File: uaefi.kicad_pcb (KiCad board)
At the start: 4 copper layers, 100 x 100 mm, 171 parts, among them J1 Conn_02x02_Odd_Even, J10 5569-16A2, J11 Conn_02x02_Odd_Even, J12 Conn_02x02_Odd_Even, J13 Conn_02x02_Odd_Even, J14 Conn_02x02_Odd_Even, J15 Conn_02x02_Odd_Even, J16 Conn_02x02_Odd_Even, J17 Conn_02x02_Odd_Even, J18 Conn_02x02_Odd_Even, J19 Conn_02x02_Odd_Even, J2 5569-20A2, J20 Conn_02x02_Odd_Even, J21 Conn_02x02_Odd_Even, J22 Conn_02x02_Odd_Even, J24 Conn_02x02_Odd_Even, J3 5569-06A2, J4 5569-08A2, J5 5569-18A2, J6 Conn_01x06, J7 Conn_01x05_Male, J8 USB_B_Mini, J9 USB_C, M1 Module-power_12and5V-0.3, M2 Module-knock-0.2, M3 Module-vr-discrete-0.5, M4 Module-vr-max9924-0.1, M5 Module-wbo-0.6, M6 Module:mega-mcu100/0.3, M7 Module-can-0.1, P1 Pad, P15 Pad, P16 Pad, P17 Pad, P18 Pad, P2 Pad, P3 Pad, P4 Pad, P5 Pad, P6 Pad, P7 Pad, P8 Pad, Q10 ISL9V3040D3ST, Q11 ISL9V3040D3ST, Q12 ISL9V3040D3ST, Q7 ISL9V3040D3ST, Q8 ISL9V3040D3ST, Q9 ISL9V3040D3ST, U1 TLE9201SG, U10 VNLD5160TR-E, U11 VNLD5160TR-E, U2 TLE9201SG, U3 MPX4/MPXH6400_MAP, U4 MAX31855KASA, U5 JDY-33, U6 VNLD5160TR-E, U7 VNLD5160TR-E, U8 VNLD5160TR-E, U9 VNLD5160TR-E

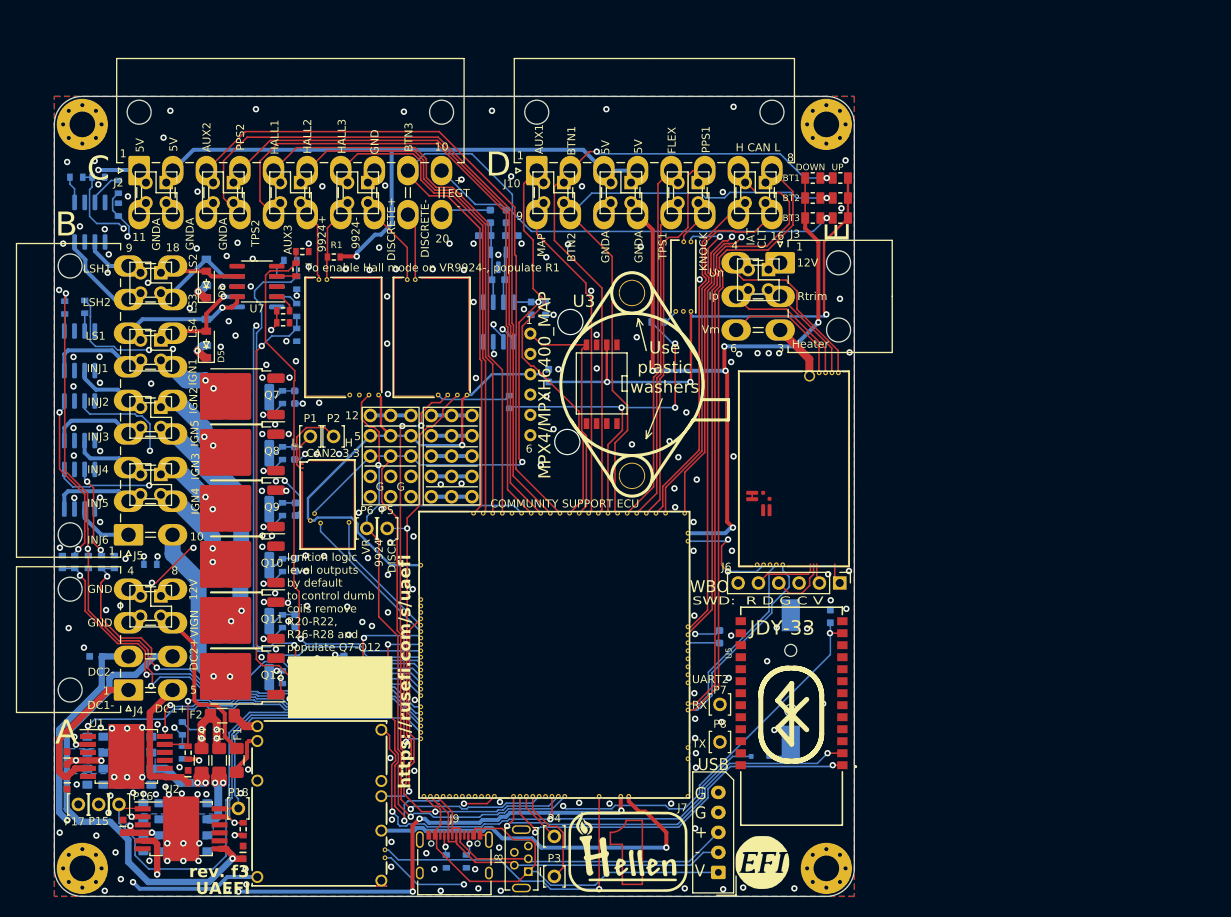
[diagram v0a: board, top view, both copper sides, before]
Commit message: uaefi-moto: PCB prepared for routing, bluetooth fix caps [skip ci]
Schematic:
- breakout pin headers J1, J11-J24 removed (never populated)
- C40 47uF on +5V and C41 470uF on +3.3VA for the JDY-33 power-up issue
- ERC 0 errors, no existing net changed, connector pins match spreadsheet

PCB:
- old Mini-Fit connectors, DC drivers, F3/F4, breakout headers and the
  routes that only led to them removed
- board enlarged to 145 x 110 mm (right: EGT/M8, top: Superseal pin depth)
- J30/J31, F11, M8, J32-J35, four MAX31855 groups, C40/C41 pre-placed
- DRC: 0 errors except library courtyard of the Superseal footprint,
  schematic parity 0, 138 unconnected items left to route

Co-Authored-By: Claude Opus 5.5 <noreply@anthropic.com>
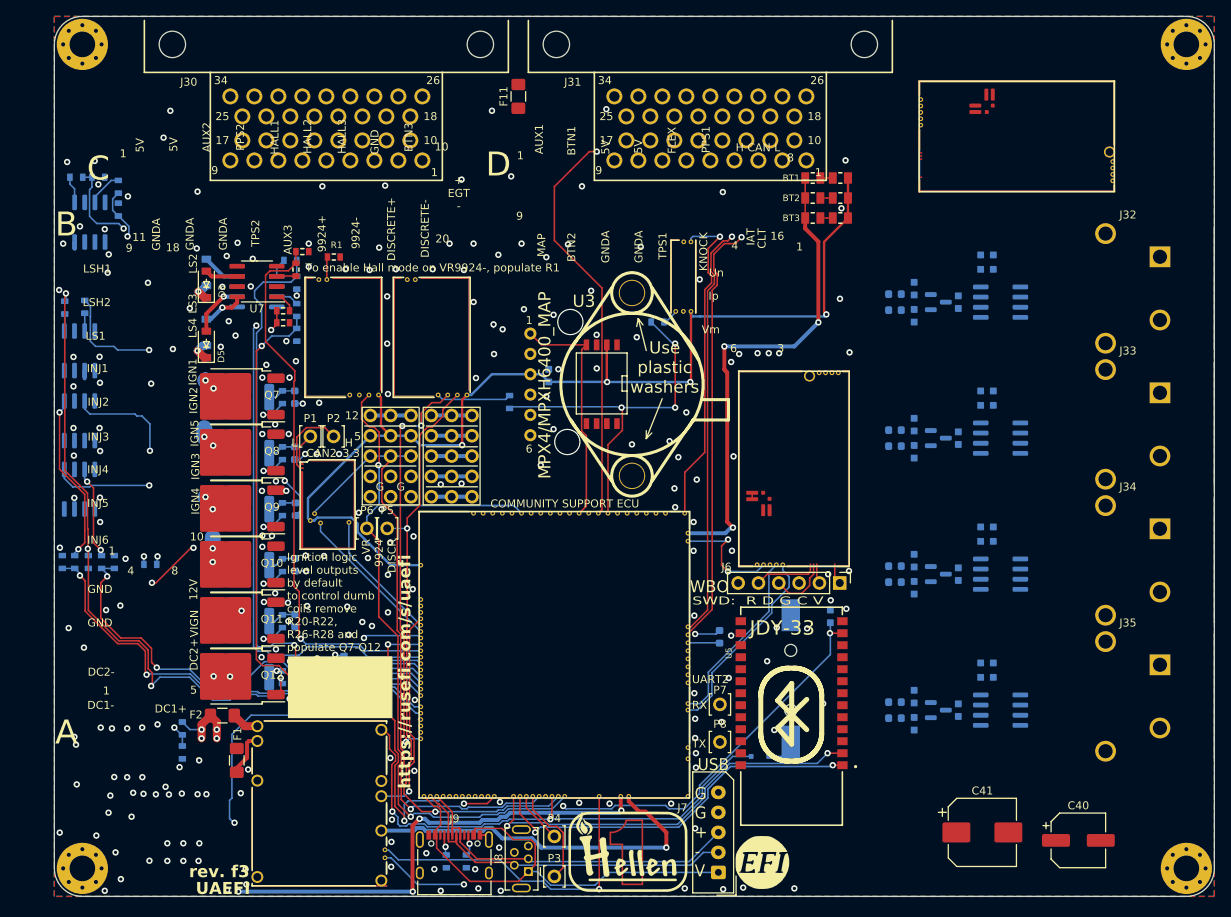
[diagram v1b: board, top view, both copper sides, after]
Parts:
- removed C1, C10, C14, C15, C16, C17, C18, C19, C2, C20, C21, C22, C23, C3, C4, C5, C6, C7, C8, C9: 10u, hellen-one-common:C0805
- removed C11, C24: 100n, hellen-one-common:C0603
- removed C12, C13, C25, C26: 10n, hellen-one-common:C0603
- removed F3, F4: Fuse, Fuse:Fuse_1206_3216Metric_Pad1.42x1.75mm_HandSolder
- removed J1, J11, J12, J13, J14, J15, J16, J17, J18, J19, J20, J21, J22, J24: Conn_02x02_Odd_Even, Connector_PinSocket_2.54mm:PinSocket_2x02_P2.54mm_Vertical
- removed J10: 5569-16A2, Connector_Molex:Molex_Mini-Fit_Jr_5569-16A2_2x08_P4.20mm_Horizontal
- removed J2: 5569-20A2, Connector_Molex:Molex_Mini-Fit_Jr_5569-20A2_2x10_P4.20mm_Horizontal
- removed J3: 5569-06A2, Connector_Molex:Molex_Mini-Fit_Jr_5569-06A2_2x03_P4.20mm_Horizontal
- removed J4: 5569-08A2, Connector_Molex:Molex_Mini-Fit_Jr_5569-08A2_2x04_P4.20mm_Horizontal
- removed J5: 5569-18A2, Connector_Molex:Molex_Mini-Fit_Jr_5569-18A2_2x09_P4.20mm_Horizontal
- removed P15, P16, P17, P18: Pad, hellen-one-common:PAD-TH
- removed R14, R9: 4.7k, hellen-one-common:R0603
- removed U1, U2: TLE9201SG, Package_SO:Infineon_PG-DSO-12-11
- added C2028: 10n, hellen-one-common:C0603, B.Cu at (157.5, 104.4)
- added C2029: 100n, hellen-one-common:C0603, B.Cu at (163.0, 102.7)
- added C2030: 10n, hellen-one-common:C0603, B.Cu at (157.5, 101.0)
- added C2031: 100n, hellen-one-common:C0603, B.Cu at (166.6, 98.6)
- added C2032: 1u, hellen-one-common:C0603, B.Cu at (166.6, 96.8)
- added C3028: 10n, hellen-one-common:C0603, B.Cu at (157.5, 121.4)
- added C3029: 100n, hellen-one-common:C0603, B.Cu at (163.0, 119.7)
- added C3030: 10n, hellen-one-common:C0603, B.Cu at (157.5, 118.0)
- added C3031: 100n, hellen-one-common:C0603, B.Cu at (166.6, 115.6)
- added C3032: 1u, hellen-one-common:C0603, B.Cu at (166.6, 113.8)
- added C40: 47uF 16V, Capacitor_SMD:CP_Elec_6.3x5.4, F.Cu at (178.0, 153.0)
- added C4028: 10n, hellen-one-common:C0603, B.Cu at (157.5, 138.4)
- added C4029: 100n, hellen-one-common:C0603, B.Cu at (163.0, 136.7)
- added C4030: 10n, hellen-one-common:C0603, B.Cu at (157.5, 135.0)
- added C4031: 100n, hellen-one-common:C0603, B.Cu at (166.6, 132.6)
- added C4032: 1u, hellen-one-common:C0603, B.Cu at (166.6, 130.8)
- added C41: 470uF 6.3V, Capacitor_SMD:CP_Elec_8x10, F.Cu at (166.0, 152.0)
- added D2008: NUP2105L, Package_TO_SOT_SMD:SOT-23, B.Cu at (160.5, 102.7)
- added D3008: NUP2105L, Package_TO_SOT_SMD:SOT-23, B.Cu at (160.5, 119.7)
- added D4008: NUP2105L, Package_TO_SOT_SMD:SOT-23, B.Cu at (160.5, 136.7)
- added F11: PTC 200mA hold, Fuse:Fuse_1206_3216Metric_Pad1.42x1.75mm_HandSolder, F.Cu at (108.0, 60.0)
- added J30: TE 6437288-1 (A, keying 1), Connectors:6437288-2, F.Cu at (84.0, 53.5)
- added J31: TE 6437288-2 (B, keying 2), Connectors:6437288-2, F.Cu at (132.0, 53.5)
- added J32: EGT1 PCC-SMP-K, moto:Omega_PCC-SMP-K, F.Cu at (188.2, 84.0)
- added J33: EGT2 PCC-SMP-K, moto:Omega_PCC-SMP-K, F.Cu at (188.2, 101.0)
- added J34: EGT3 PCC-SMP-K, moto:Omega_PCC-SMP-K, F.Cu at (188.2, 118.0)
- added J35: EGT4 PCC-SMP-K, moto:Omega_PCC-SMP-K, F.Cu at (188.2, 135.0)
- added L2001: 470R@100MHz, Inductor_SMD:L_0603_1608Metric, B.Cu at (155.1, 101.7)
- added L2002: 470R@100MHz, Inductor_SMD:L_0603_1608Metric, B.Cu at (155.1, 103.7)
- added L3001: 470R@100MHz, Inductor_SMD:L_0603_1608Metric, B.Cu at (155.1, 118.7)
- added L3002: 470R@100MHz, Inductor_SMD:L_0603_1608Metric, B.Cu at (155.1, 120.7)
- added L4001: 470R@100MHz, Inductor_SMD:L_0603_1608Metric, B.Cu at (155.1, 135.7)
- added L4002: 470R@100MHz, Inductor_SMD:L_0603_1608Metric, B.Cu at (155.1, 137.7)
- added M8: Module-wbo-0.6, hellen-one-wbo-0.6:wbo, F.Cu at (158.0, 72.0)
- added U2004: MAX31855KASA, Package_SO:SOIC-8_3.9x4.9mm_P1.27mm, B.Cu at (168.3, 102.7)
- added U3004: MAX31855KASA, Package_SO:SOIC-8_3.9x4.9mm_P1.27mm, B.Cu at (168.3, 119.7)
- added U4004: MAX31855KASA, Package_SO:SOIC-8_3.9x4.9mm_P1.27mm, B.Cu at (168.3, 136.7)
- R39: value DNP -> 4.7k
- moved U4 62.8 mm to (168.3, 85.7), turned to 0 degrees
- moved C29 57.6 mm to (163.0, 85.7), turned to 90 degrees
- moved C31 57.2 mm to (166.6, 81.6), turned to 180 degrees
- moved C32 55.6 mm to (166.6, 79.8), turned to 180 degrees
- moved D8 55.2 mm to (160.5, 85.7), turned to 0 degrees
- moved C28 54.6 mm to (157.5, 87.4), turned to 90 degrees
- moved L2 51.9 mm to (155.1, 86.7), turned to 0 degrees
- moved C30 50.7 mm to (157.5, 84.0), turned to -90 degrees
- moved L1 49.5 mm to (155.1, 84.7), turned to 0 degrees
- moved H4 46.1 mm to (191.5, 53.5)
- moved H3 45.0 mm to (191.5, 156.5)
- moved H1 10.0 mm to (53.5, 53.5)
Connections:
- net /OUT_IGN5 renamed /Ignition/OUT5
- net /OUT_IGN6 renamed /Ignition/OUT6
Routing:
- net +5VP: track 201.8 -> 0.11 mm, vias 3 -> 0
- net +12V_RAW: track 255.4 -> 130.3 mm
- net /IN_BUTTON3: track 109.2 -> 1.55 mm, vias 1 -> 0
- net GNDA: track 155.1 -> 60.7 mm, vias 5 -> 3
- net /IN_TPS2: track 88.5 -> 0.00 mm
- net /IN_AUX2: track 85.1 -> 0.00 mm
- net /IN_AUX3: track 81.5 -> 0.00 mm
- net /CAN+: track 103.0 -> 22.8 mm
- net /IN_PPS2: track 78.2 -> 0.00 mm
- net /CAN-: track 102.2 -> 24.4 mm
- net /IN_BUTTON2: track 76.6 -> 1.55 mm, vias 1 -> 0
- net /IN_HALL1: track 70.3 -> 0.00 mm
- net /IN_HALL2: track 64.9 -> 0.00 mm
- net /DC1_DIR: track 64.0 -> 0.00 mm, vias 1 -> 0
- net /DC1_PWM: track 61.0 -> 0.30 mm, vias 2 -> 0
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- removed copper zone on B.Cu, net /DC Driver 1/PWR
- removed copper zone on B.Cu, net /DC Driver 2/PWR
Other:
- board size 100 x 100 mm -> 145 x 110 mm
- board text removed: "DOWN"
- board text removed: "E"
- board text removed: "Heater"
- board text removed: "Rtrim"
- board text removed: "UP"
